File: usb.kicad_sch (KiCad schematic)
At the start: 1 part

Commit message: write some things down
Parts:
- U1: renamed from U?; value MCIMX6YxxVMxxxx -> MCIMX6Y2DVM09AB; Manufacturer (none) -> NXP; MfgPartNo (none) -> MCIMX6Y2DVM09AB; Vendor (none) -> Digi-Key; VendorPartNo (none) -> 568-14995-ND
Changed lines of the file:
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@@
   (symbol (lib_id "catfood:MCIMX6YxxVMxxxx") (at 76.2 68.58 0) (unit 6)
     (in_bom yes) (on_board yes) (fields_autoplaced)
-    (property "Reference" "U?" (id 0) (at 77.47 36.83 0))
-    (property "Value" "MCIMX6YxxVMxxxx" (id 1) (at 77.47 39.37 0))
+    (property "Reference" "U1" (id 0) (at 77.47 36.83 0))
+    (property "Value" "MCIMX6Y2DVM09AB" (id 1) (at 77.47 39.37 0))
     (property "Footprint" "" (id 2) (at 66.04 49.53 0)
       (effects (font (size 1.27 1.27)) hide)
@@
       (effects (font (size 1.27 1.27)) hide)
     )
+    (property "Manufacturer" "NXP" (id 4) (at 77.47 46.99 0)
+      (effects (font (size 1.27 1.27)) hide)
+    )
+    (property "MfgPartNo" "MCIMX6Y2DVM09AB" (id 5) (at 77.47 49.53 0)
+      (effects (font (size 1.27 1.27)) hide)
+    )
+    (property "Vendor" "Digi-Key" (id 6) (at 77.47 52.07 0)
+      (effects (font (size 1.27 1.27)) hide)
+    )
+    (property "VendorPartNo" "568-14995-ND" (id 7) (at 77.47 54.61 0)
+      (effects (font (size 1.27 1.27)) hide)
+    )

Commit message: USB, GPIO
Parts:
- added C? (x2): 1uF 0603, symbol Device:C_Small
- added C?: 10uF 0805, symbol Device:C_Small
- added C?: 0.1uF 0402, symbol Device:C_Small
- added D?: uClamp0571P, Diode_SMD:D_SMF, symbol Device:D_Zener
- added D? (x2): RCLAMP0582B, Package_TO_SOT_SMD:SOT-416, symbol Power_Protection:RCLAMP0582B
- added D?: uClamp0571P, symbol Device:D_Zener
- added J?: USB4110, symbol Connector:USB_C_Receptacle_USB2.0
- added J?: USB_A, symbol Connector:USB_A
- added R? (x2): 5.1k 0402, symbol Device:R_Small
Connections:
- net at U1.R12 (VDD_USB_CAP): now also C?.1, C?.1
- net VDD_5V: now reaches U1.T12 (USB_OTG1_VBUS)
- net VDD_5V: now also U1.U12 (USB2_OTG2_VBUS), C?.1, C?.1, D?.1 (K), D?.1 (K), J?.1 (VBUS), J?.A4 (VBUS), J?.A9 (VBUS), J?.B4 (VBUS), J?.B9 (VBUS)
- net USB_OTG2_DN: now reaches U1.T13 (USB_OTG2_DN)
- net USB_OTG2_DN: now also D?.2 (K2), J?.2 (D-)
- net USB_OTG1_DN: now reaches U1.T15 (USB_OTG1_DN)
- net USB_OTG1_DN: now also D?.1 (K1), J?.A7 (D-), J?.B7 (D-)
- net USB_OTG2_DP: now reaches U1.U13 (USB_OTG2_DP)
- net USB_OTG2_DP: now also D?.1 (K1), J?.3 (D+)
- net USB_OTG1_DP: now reaches U1.U15 (USB_OTG1_DP)
- net USB_OTG1_DP: now also D?.2 (K2), J?.A6 (D+), J?.B6 (D+)
- new net: J?.A5 (CC1), R?.1
- new net: J?.B5 (CC2), R?.1
- new net GND: C?.2, C?.2, C?.2, C?.2, D?.2 (A), D?.2 (A), D?.3 (A), D?.3 (A), J?.4 (GND), J?.5 (Shield), J?.A1 (GND), J?.A12 (GND), J?.B1 (GND), J?.B12 (GND), J?.S1 (SHIELD), R?.2, R?.2
- no-connect marks 0 -> 3
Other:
- note added: "Power/Bootloader/Console"
- note added: "Rd: 5V 3A"
- note added: "USB 2.0 Host Port"

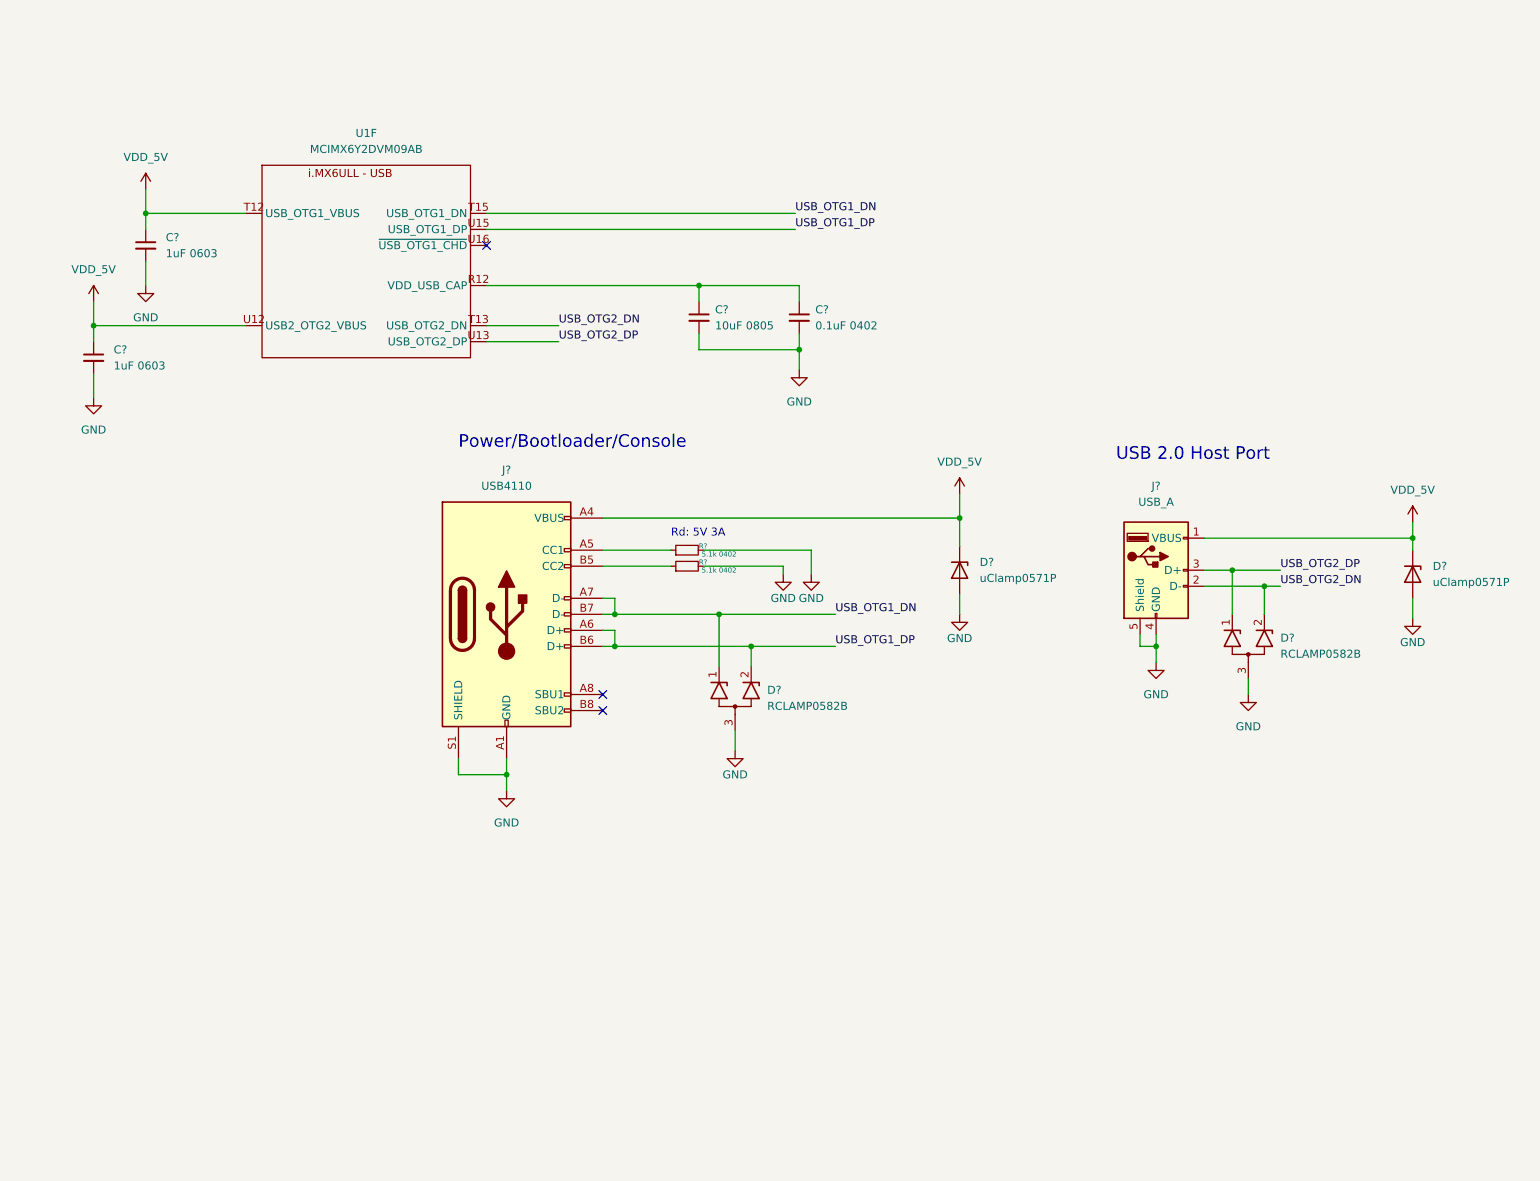
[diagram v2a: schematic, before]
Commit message: USB host port capacitance, load switch
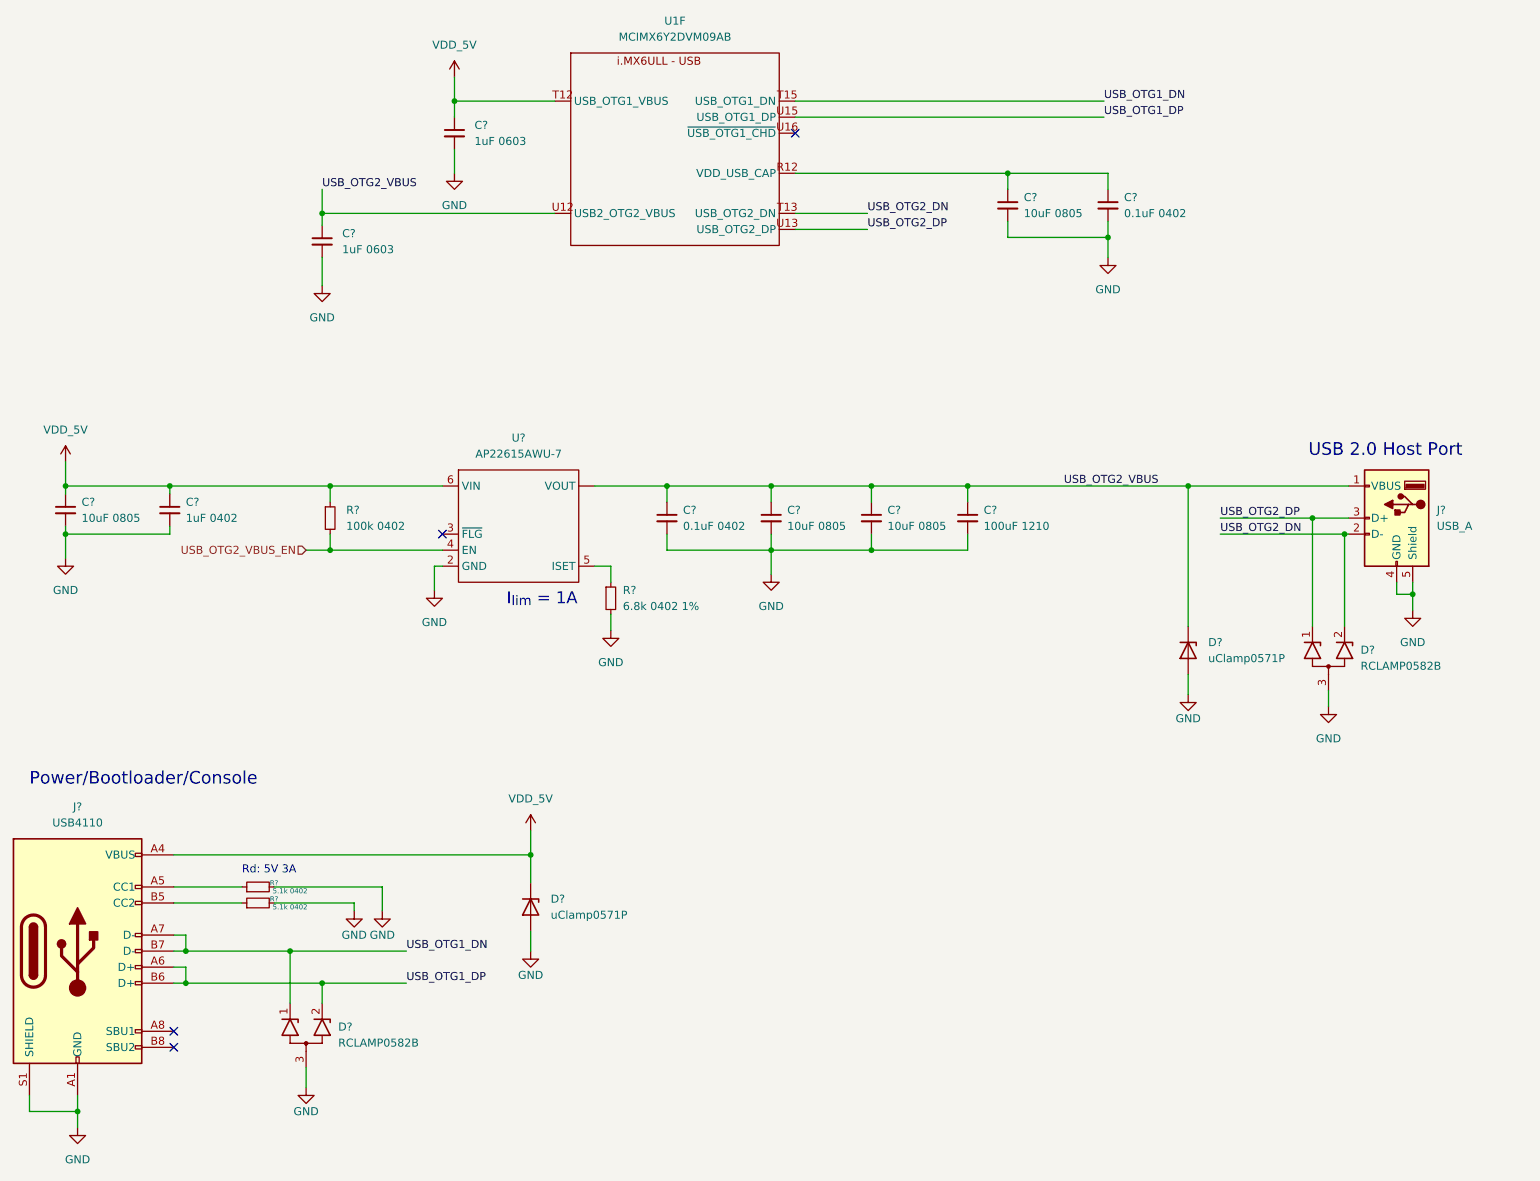
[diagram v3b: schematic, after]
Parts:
- removed J?: USB_A, symbol Connector:USB_A
- added C?: 1uF 0402, symbol Device:C_Small
- added C? (x3): 10uF 0805, symbol Device:C_Small
- added C?: 0.1uF 0402, symbol Device:C_Small
- added C?: 100uF 1210, symbol Device:C_Small
- added J?: USB_A, symbol Connector:USB_A
- added R?: 100k 0402, symbol Device:R_Small
- added R?: 6.8k 0402 1%, symbol Device:R_Small
- added U?: AP22615AWU-7, symbol catfood:AP22615AWU-7
- D?: footprint (none) -> Diode_SMD:D_SMF
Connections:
- net GND: now also C?.2, C?.2, C?.2, C?.2, C?.2, C?.2, J?.4 (GND), J?.5 (Shield), R?.2, U?.2 (GND)
- net USB_OTG2_DN: now also J?.2 (D-)
- net USB_OTG2_DP: now also J?.3 (D+)
- net VDD_5V: now also C?.1, C?.1, R?.1, U?.6 (VIN); no longer C?.1, D?.1 (K), U1.U12 (USB2_OTG2_VBUS)
- new net: R?.1, U?.5 (ISET)
- new net USB_OTG2_VBUS: C?.1, C?.1, C?.1, C?.1, C?.1, D?.1 (K), J?.1 (VBUS), U1.U12 (USB2_OTG2_VBUS), U?. (VOUT)
- new net USB_OTG2_VBUS_EN: R?.2, U?.4 (EN)
- no-connect marks 3 -> 4
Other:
- note added: "I_{lim} = 1A"
- moved on the sheet: C?, D?, J?, R?, U1F

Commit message: Annotation
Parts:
- gave numbers to parts that had none: 21
- renumbered U1 to U4
